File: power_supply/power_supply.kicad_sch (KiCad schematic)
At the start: 8 parts, among them J1 Input, J2 Input

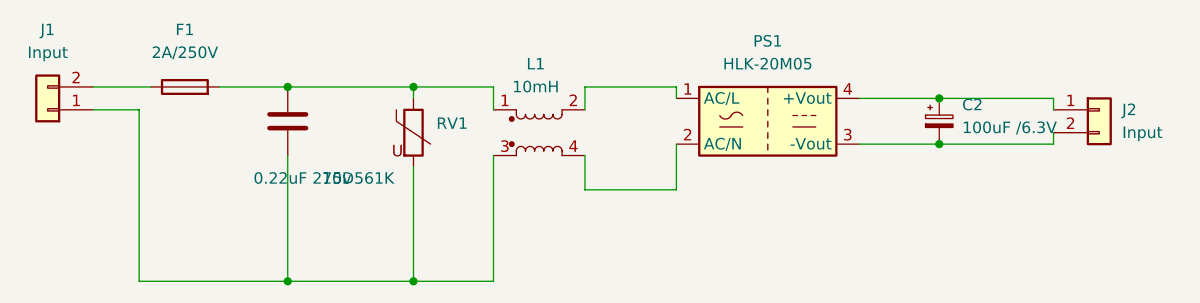
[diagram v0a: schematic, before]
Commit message: update powersupply pcb
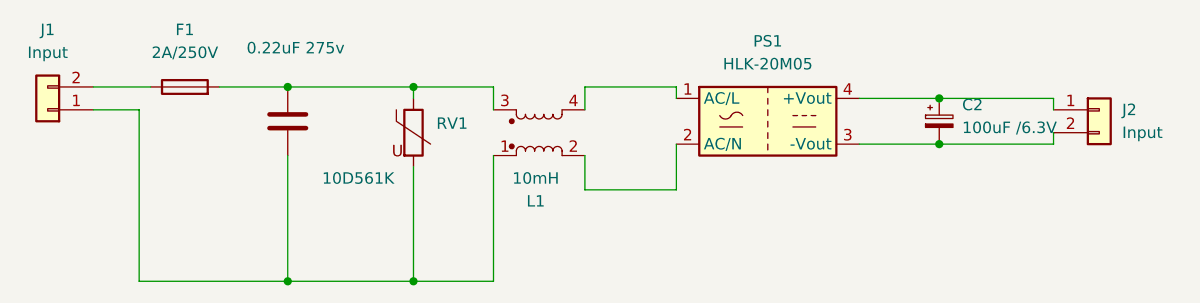
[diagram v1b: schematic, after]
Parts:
- C1: footprint Capacitor_SMD:C_1206_3216Metric_Pad1.33x1.80mm_HandSolder -> B32023B3104K000:CAPRR2250W80L2650T1050H1650
- C2: footprint (none) -> Capacitor_THT:CP_Radial_D5.0mm_P2.50mm
- J1: footprint Connector_Molex:Molex_Micro-Fit_3.0_43650-0215_1x02_P3.00mm_Vertical -> Connector_TE-Connectivity:TE_826576-2_1x02_P3.96mm_Vertical
- RV1: footprint Varistor:Bourns_Inc.-MOV-14D471K-MFG -> eec:Bourns_Inc.-MOV-14D471K-MFG
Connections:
- net at C1.1, F1.2, RV1.1: now also L1.3; no longer L1.1
- net at C1.2, J1.1 (Pin_1), RV1.2: now also L1.1; no longer L1.3
- net at L1.2: now also PS1.2 (AC/N); no longer PS1.1 (AC/L)
- net at L1.4: now also PS1.1 (AC/L); no longer PS1.2 (AC/N)
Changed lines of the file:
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@@
 			)
 		)
-		(property "Footprint" "Varistor:Bourns_Inc.-MOV-14D471K-MFG"
+		(property "Footprint" "eec:Bourns_Inc.-MOV-14D471K-MFG"
 			(at 127.762 110.49 90)
 			(effects
@@
 		(lib_id "Device:L_Coupled")
 		(at 143.51 110.49 0)
-		(unit 1)
-		(exclude_from_sim no)
-		(in_bom yes)
-		(on_board yes)
-		(dnp no)
-		(fields_autoplaced yes)
+		(mirror x)
+		(unit 1)
+		(exclude_from_sim no)
+		(in_bom yes)
+		(on_board yes)
+		(dnp no)
 		(property "Reference" "L1"
-			(at 143.129 102.87 0)
+			(at 143.129 118.11 0)
 			(effects
 				(font
@@
 		)
 		(property "Value" "10mH"
-			(at 143.129 105.41 0)
+			(at 143.129 115.57 0)
 			(effects
 				(font
@@
 		)
 		(property "Value" "0.22uF 275v"
-			(at 111.76 115.57 0)
-			(effects
-				(font
-					(size 1.27 1.27)
-				)
-				(justify left)
-			)
-		)
-		(property "Footprint" "Capacitor_SMD:C_1206_3216Metric_Pad1.33x1.80mm_HandSolder"
+			(at 110.998 101.092 0)
+			(effects
+				(font
+					(size 1.27 1.27)
+				)
+				(justify left)
+			)
+		)
+		(property "Footprint" "B32023B3104K000:CAPRR2250W80L2650T1050H1650"
 			(at 116.5352 113.03 0)
 			(effects
@@
 			)
 		)
-		(property "Footprint" ""
+		(property "Footprint" "Capacitor_THT:CP_Radial_D5.0mm_P2.50mm"
 			(at 187.96 109.22 0)
 			(effects
@@
 			)
 		)
-		(property "Footprint" "Connector_Molex:Molex_Micro-Fit_3.0_43650-0215_1x02_P3.00mm_Vertical"
+		(property "Footprint" "Connector_TE-Connectivity:TE_826576-2_1x02_P3.96mm_Vertical"
 			(at 88.9 107.95 0)
 			(effects
